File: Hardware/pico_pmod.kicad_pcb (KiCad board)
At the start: 2 copper layers, 66 x 43.2 mm, 2 parts, among them J1 Conn_02x15_Odd_Even, U1 Pico

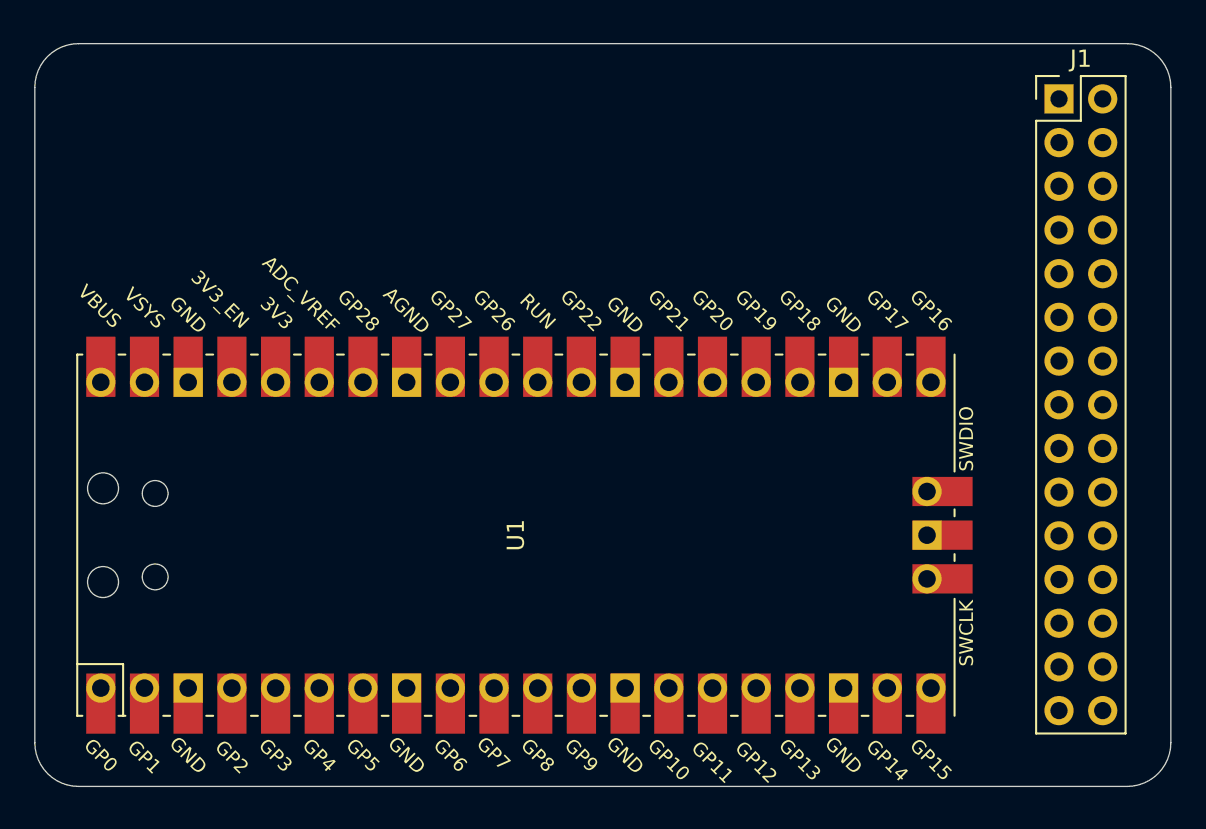
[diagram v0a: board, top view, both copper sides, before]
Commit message: add power pin headers and initial layout work
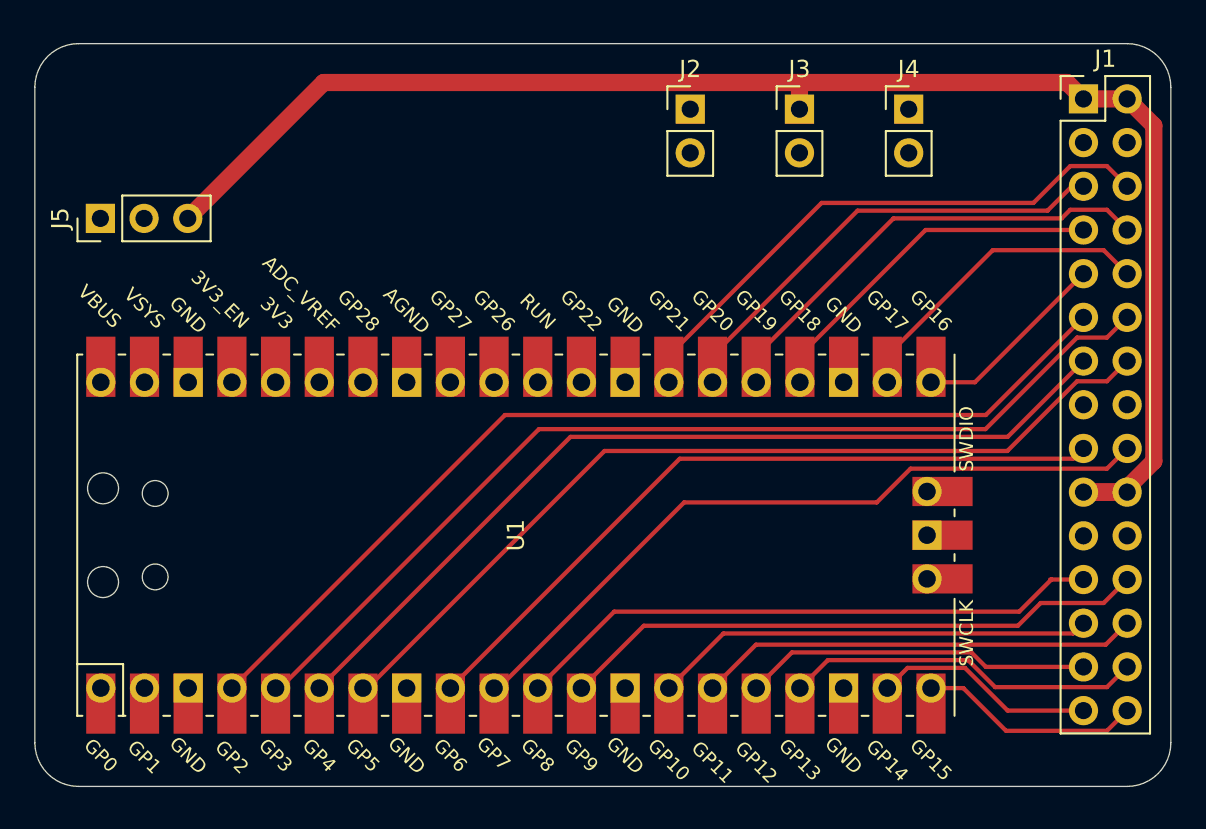
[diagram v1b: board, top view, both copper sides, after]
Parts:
- added J2: Conn_01x02, Connector_PinHeader_2.54mm:PinHeader_1x02_P2.54mm_Vertical, F.Cu at (152.4, 77.5)
- added J3: Conn_01x02, Connector_PinHeader_2.54mm:PinHeader_1x02_P2.54mm_Vertical, F.Cu at (158.8, 77.5)
- added J4: Conn_01x02, Connector_PinHeader_2.54mm:PinHeader_1x02_P2.54mm_Vertical, F.Cu at (165.1, 77.5)
- added J5: Conn_01x03, Connector_PinHeader_2.54mm:PinHeader_1x03_P2.54mm_Vertical, F.Cu at (118.1, 83.8)
- moved J1 1.42 mm to (175.3, 76.9)
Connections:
- net Net-(U1-Pad1) renamed GPIO_00
- net Net-(U1-Pad2) renamed GPIO_01
- net Net-(U1-Pad29) renamed GPIO_22
- J1 pad 1: Net-(J1-Pad1) -> +3V3
- J1 pad 10: Net-(J1-Pad10) -> GPIO_17
- J1 pad 11: Net-(J1-Pad11) -> GPIO_02
- J1 pad 12: Net-(J1-Pad12) -> GPIO_03
- J1 pad 13: Net-(J1-Pad13) -> GPIO_04
- J1 pad 14: Net-(J1-Pad14) -> GPIO_05
- J1 pad 15: Net-(J1-Pad15) -> +5V
- J1 pad 16: Net-(J1-Pad16) -> GND
- J1 pad 17: Net-(J1-Pad17) -> GPIO_06
- J1 pad 18: Net-(J1-Pad18) -> GPIO_07
- J1 pad 19: Net-(J1-Pad19) -> +3V3
- J1 pad 2: Net-(J1-Pad2) -> +3V3
- J1 pad 20: Net-(J1-Pad20) -> +3V3
- J1 pad 21: Net-(J1-Pad21) -> GND
- J1 pad 22: Net-(J1-Pad22) -> GND
- J1 pad 23: Net-(J1-Pad23) -> GPIO_08
- J1 pad 24: Net-(J1-Pad24) -> GPIO_09
- J1 pad 25: Net-(J1-Pad25) -> GPIO_10
- J1 pad 26: Net-(J1-Pad26) -> GPIO_11
- J1 pad 27: Net-(J1-Pad27) -> GPIO_12
- J1 pad 28: Net-(J1-Pad28) -> GPIO_13
- J1 pad 29: Net-(J1-Pad29) -> GPIO_14
- J1 pad 3: Net-(J1-Pad3) -> GND
- J1 pad 30: Net-(J1-Pad30) -> GPIO_15
- J1 pad 4: Net-(J1-Pad4) -> GND
- J1 pad 5: Net-(J1-Pad5) -> GPIO_20
- J1 pad 6: Net-(J1-Pad6) -> GPIO_21
- J1 pad 7: Net-(J1-Pad7) -> GPIO_18
- J1 pad 8: Net-(J1-Pad8) -> GPIO_19
- J1 pad 9: Net-(J1-Pad9) -> GPIO_16
- U1 pad 10: Net-(U1-Pad10) -> GPIO_07
- U1 pad 11: Net-(U1-Pad11) -> GPIO_08
- U1 pad 12: Net-(U1-Pad12) -> GPIO_09
- U1 pad 13: Net-(U1-Pad13) -> GND
- U1 pad 14: Net-(U1-Pad14) -> GPIO_10
- U1 pad 15: Net-(U1-Pad15) -> GPIO_11
- U1 pad 16: Net-(U1-Pad16) -> GPIO_12
- U1 pad 17: Net-(U1-Pad17) -> GPIO_13
- U1 pad 18: Net-(U1-Pad18) -> GND
- U1 pad 19: Net-(U1-Pad19) -> GPIO_14
- U1 pad 20: Net-(U1-Pad20) -> GPIO_15
- U1 pad 21: Net-(U1-Pad21) -> GPIO_16
- U1 pad 22: Net-(U1-Pad22) -> GPIO_17
- U1 pad 23: Net-(U1-Pad23) -> GND
- U1 pad 24: Net-(U1-Pad24) -> GPIO_18
- U1 pad 25: Net-(U1-Pad25) -> GPIO_19
- U1 pad 26: Net-(U1-Pad26) -> GPIO_20
- U1 pad 27: Net-(U1-Pad27) -> GPIO_21
- U1 pad 28: Net-(U1-Pad28) -> GND
- U1 pad 3: Net-(U1-Pad3) -> GND
- U1 pad 36: Net-(U1-Pad36) -> Pico_3V3
- U1 pad 37: Net-(U1-Pad37) -> Pico_3v3_EN
- U1 pad 38: Net-(U1-Pad38) -> GND
- U1 pad 39: Net-(U1-Pad39) -> Pico_VSYS
- U1 pad 4: Net-(U1-Pad4) -> GPIO_02
- U1 pad 40: Net-(U1-Pad40) -> Pico_VBUS
- U1 pad 42: Net-(U1-Pad42) -> GND
- U1 pad 5: Net-(U1-Pad5) -> GPIO_03
- U1 pad 6: Net-(U1-Pad6) -> GPIO_04
- U1 pad 7: Net-(U1-Pad7) -> GPIO_05
- U1 pad 8: Net-(U1-Pad8) -> GND
- U1 pad 9: Net-(U1-Pad9) -> GPIO_06
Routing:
- net +3V3: track 0.00 -> 89.0 mm
- net GPIO_03: track 0.00 -> 58.4 mm
- net GPIO_02: track 0.00 -> 58.4 mm
- net GPIO_04: track 0.00 -> 52.3 mm
- net GPIO_05: track 0.00 -> 52.3 mm
- net GPIO_07: track 0.00 -> 42.6 mm
- net GPIO_06: track 0.00 -> 42.6 mm
- net GPIO_08: track 0.00 -> 34.4 mm
- net GPIO_09: track 0.00 -> 34.3 mm
- net GPIO_21: track 0.00 -> 33.2 mm
- net GPIO_20: track 0.00 -> 27.2 mm
- net GPIO_19: track 0.00 -> 27.1 mm
- net GPIO_11: track 0.00 -> 25.7 mm
- net GPIO_10: track 0.00 -> 25.7 mm
- net GPIO_18: track 0.00 -> 21.1 mm
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
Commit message: finish layout, start of silk screen
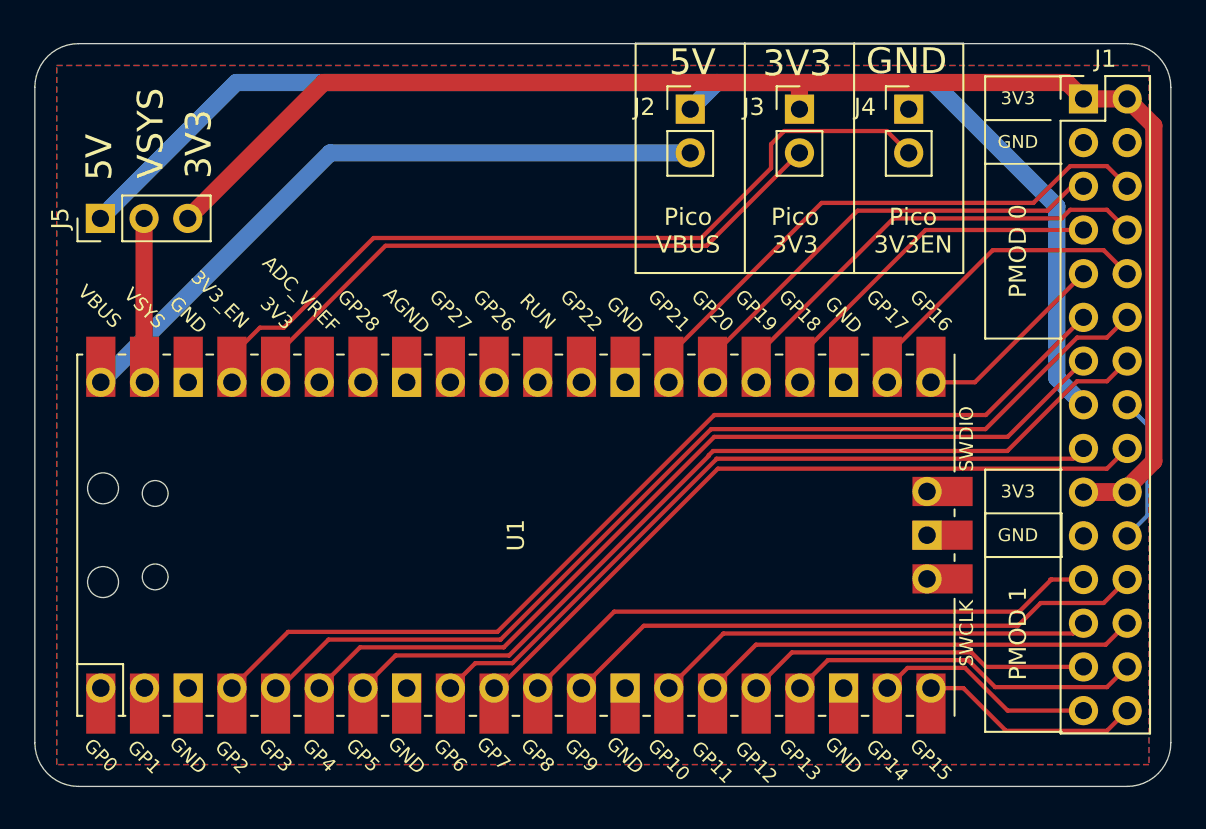
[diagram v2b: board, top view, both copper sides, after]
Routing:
- net +5V: track 0.00 -> 76.2 mm
- net Pico_3v3_EN: track 0.00 -> 47.6 mm
- net Pico_VBUS: track 0.00 -> 39.8 mm
- net Pico_3V3: track 0.00 -> 36.9 mm
- net Pico_VSYS: track 0.00 -> 9.54 mm
- net GND: track 0.00 -> 8.59 mm
- added copper zone on B.Cu, net GND
- added copper zone on F.Cu, net GND
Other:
- board text added: "3V3"
- board text added: "5V"
- board text added: "GND"
- board text added: "PMOD 0"
- board text added: "PMOD 1"
- board text added: "Pico 3V3"
- board text added: "Pico 3V3EN"
- board text added: "Pico VBUS"
- board text added: "VSYS"
